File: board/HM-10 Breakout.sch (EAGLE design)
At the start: 19 parts, among them U1 V_REG_LDOSMD

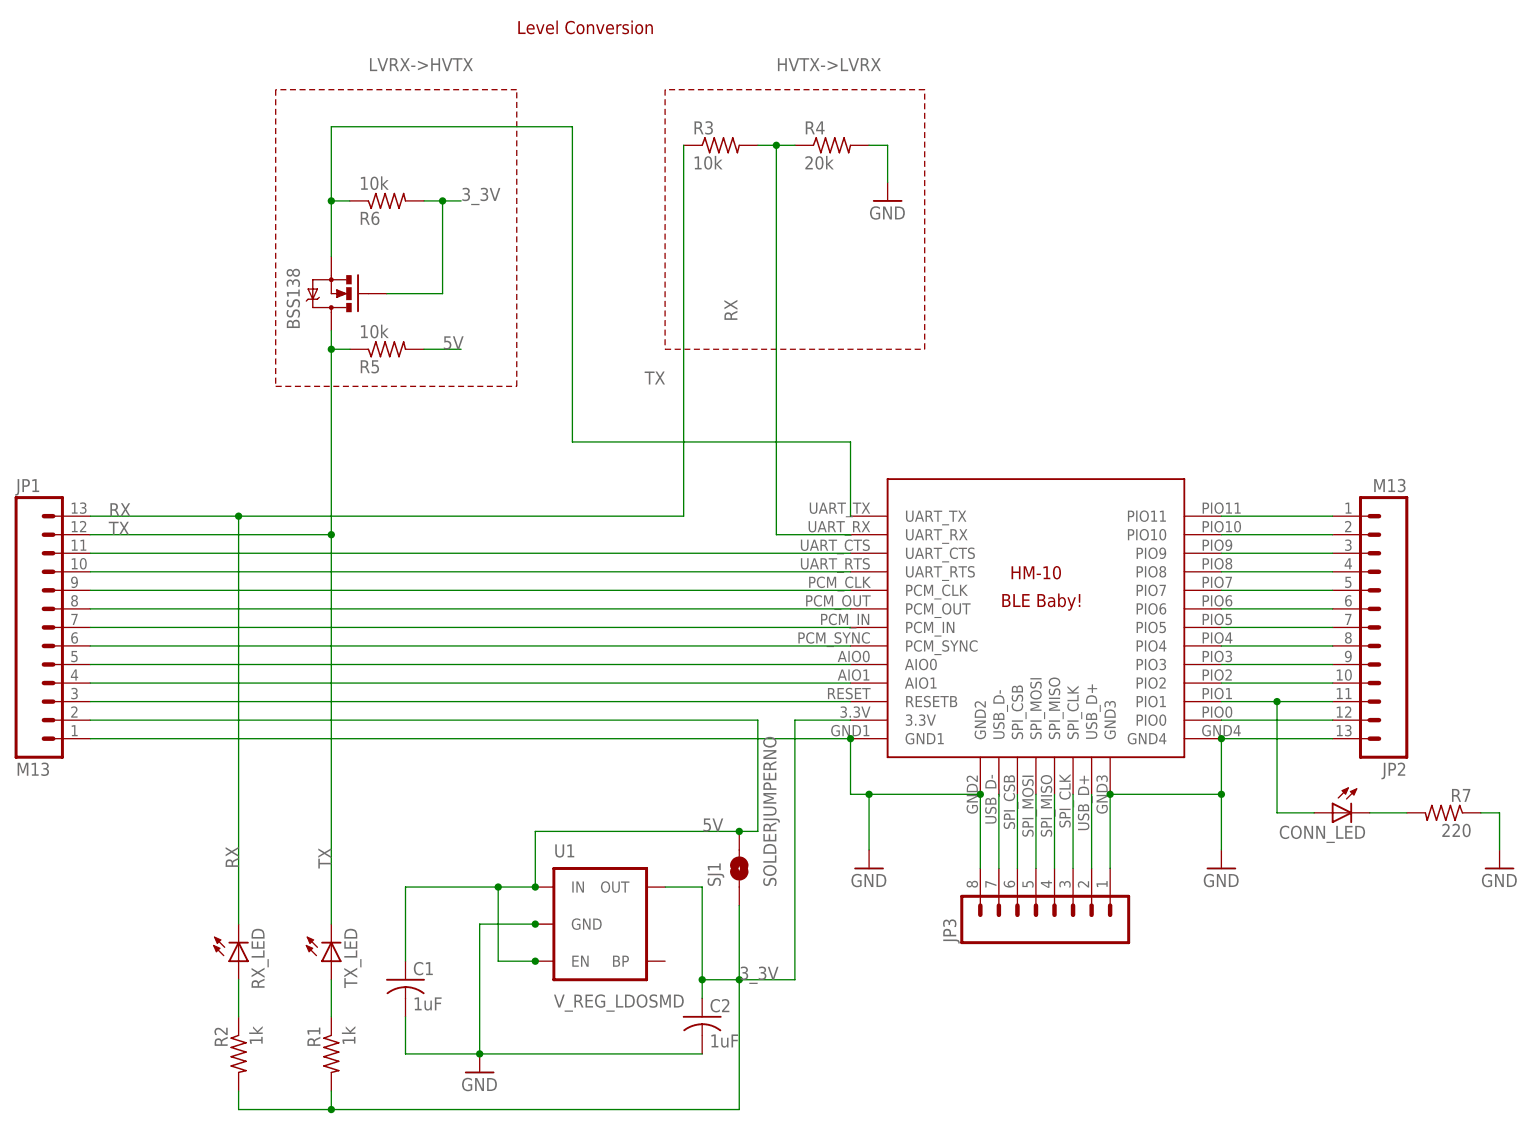
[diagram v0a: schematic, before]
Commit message: Overhaul PCB
Cleanup typography on silkscreen
Remove no connection lines
Replace HM-10 Eagle part with a more faithful version
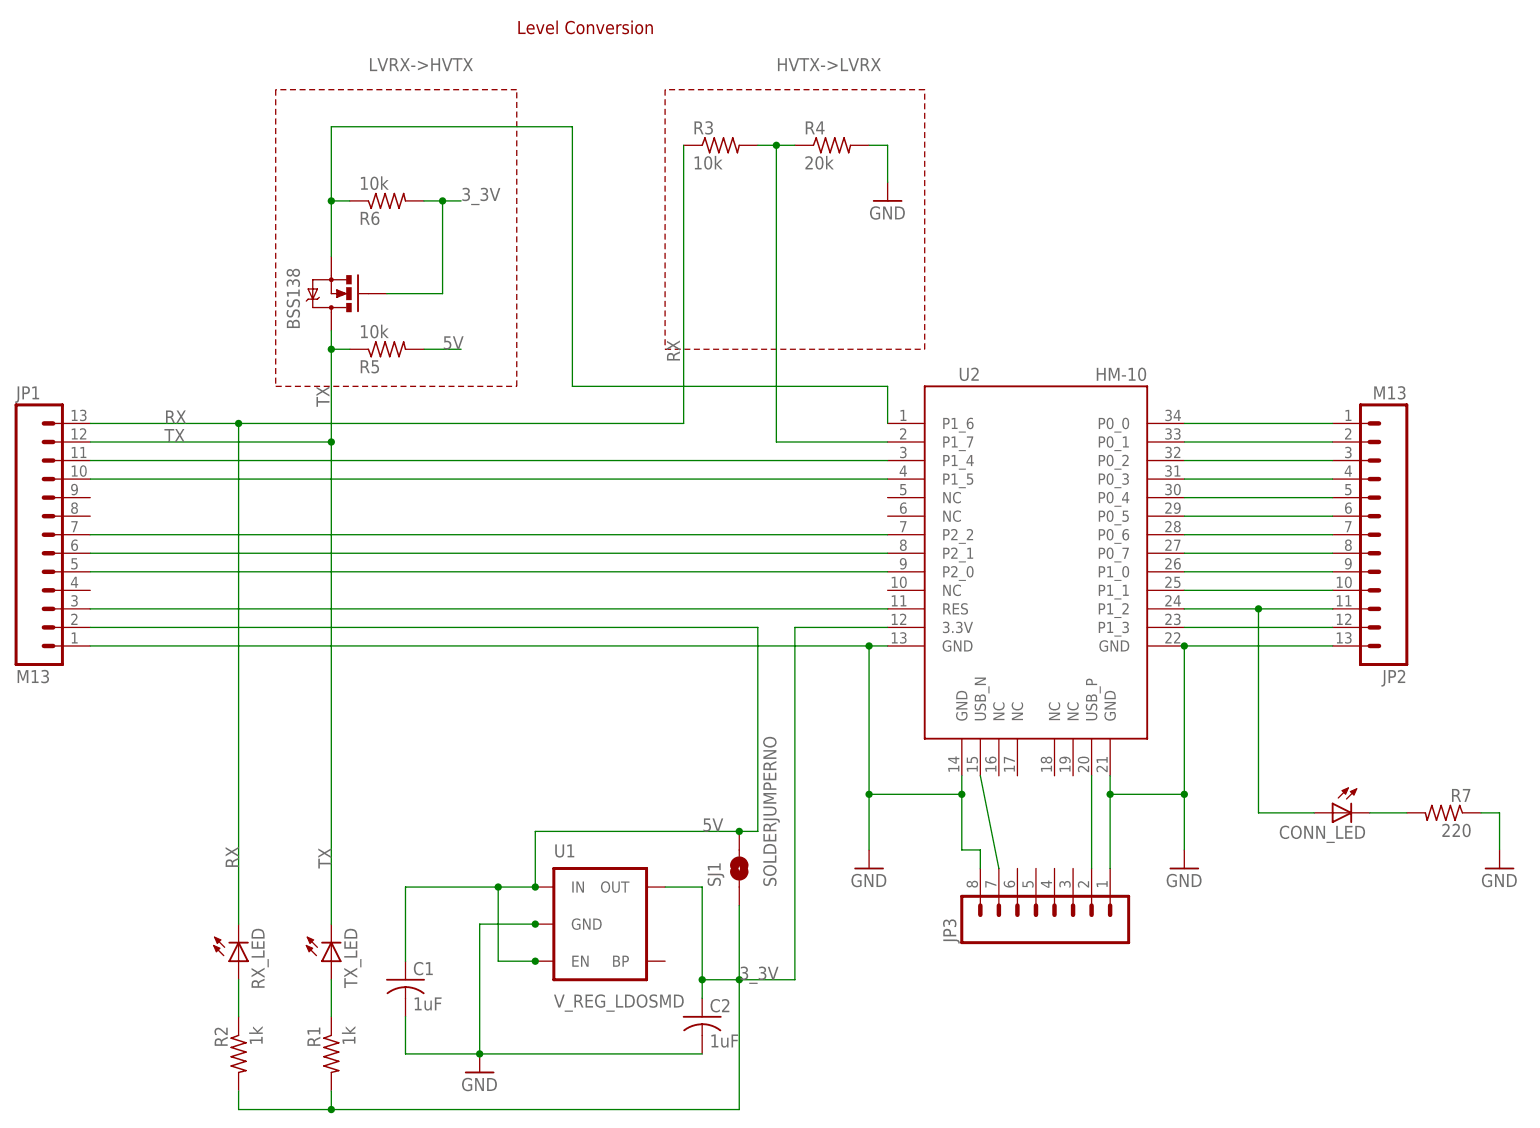
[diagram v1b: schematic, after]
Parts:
- removed U$1: BLE-HM-10, Random parts:BLE-HM-10
- added U2: HM-10, HM-10_BLE:HM-10
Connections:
- removed net N$25: JP2.12, U$1.PIO0
- removed net N$28: JP3.2, U$1.USB_D+
- removed net N$29: JP3.3, U$1.SPI_CLK
- removed net N$30: JP3.4, U$1.SPI_MISO
- removed net N$31: JP3.5, U$1.SPI_MOSI
- removed net N$32: JP3.6, U$1.SPI_CSB
- removed net N$33: JP3.7, U$1.USB_D-
- net 3_3V: now also U2.3.3V; no longer U$1.3.3V
- net GND: now also U2.GND@1, U2.GND@2, U2.GND@3, U2.GND@4; no longer U$1.GND1, U$1.GND2, U$1.GND3, U$1.GND4
- net HVTX->LVRX: now also U2.P1_7; no longer U$1.UART_RX
- net LVRX->HVTX: now also U2.P1_6; no longer U$1.UART_TX
- net N$10: now also U2.P1_5; no longer U$1.UART_RTS
- net N$11: now also U2.P1_4; no longer U$1.UART_CTS
- net N$14: now also JP2.9, U2.P1_0; no longer JP2.1, U$1.PIO11
- net N$15: now also JP2.8, U2.P0_7; no longer JP2.2, U$1.PIO10
- net N$16: now also JP2.7, U2.P0_6; no longer JP2.3, U$1.PIO9
- net N$17: now also JP2.6, U2.P0_5; no longer JP2.4, U$1.PIO8
- net N$18: now also U2.P0_4; no longer U$1.PIO7
- net N$19: now also JP2.4, U2.P0_3; no longer JP2.6, U$1.PIO6
- net N$2: now also U2.P1_2; no longer U$1.PIO1
- net N$20: now also JP2.3, U2.P0_2; no longer JP2.7, U$1.PIO5
- net N$21: now also JP2.2, U2.P0_1; no longer JP2.8, U$1.PIO4
- net N$22: now also JP2.1, U2.P0_0; no longer JP2.9, U$1.PIO3
- net N$23: now also JP2.12, U2.P1_3; no longer JP2.10, U$1.PIO2
- net N$3: now also U2.RES; no longer U$1.RESETB
- net N$4: now also JP3.7, U2.USB_N; no longer JP1.4, U$1.AIO1
- net N$5: now also JP1.7, U2.P2_2; no longer JP1.5, U$1.AIO0
- net N$6: now also JP1.5, U2.P2_0; no longer JP1.6, U$1.PCM_SYNC
- net N$7: now also JP1.6, U2.P2_1; no longer JP1.7, U$1.PCM_IN
- net N$8: now also JP2.10, U2.P1_1; no longer JP1.8, U$1.PCM_OUT
- net N$9: now also JP3.2, U2.USB_P; no longer JP1.9, U$1.PCM_CLK
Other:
- moved on the sheet: JP1, JP2

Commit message: Shrink board
Remove top row of pins
Change silkscreen to note change to SPI over USB
Add version number and text to silkscreen
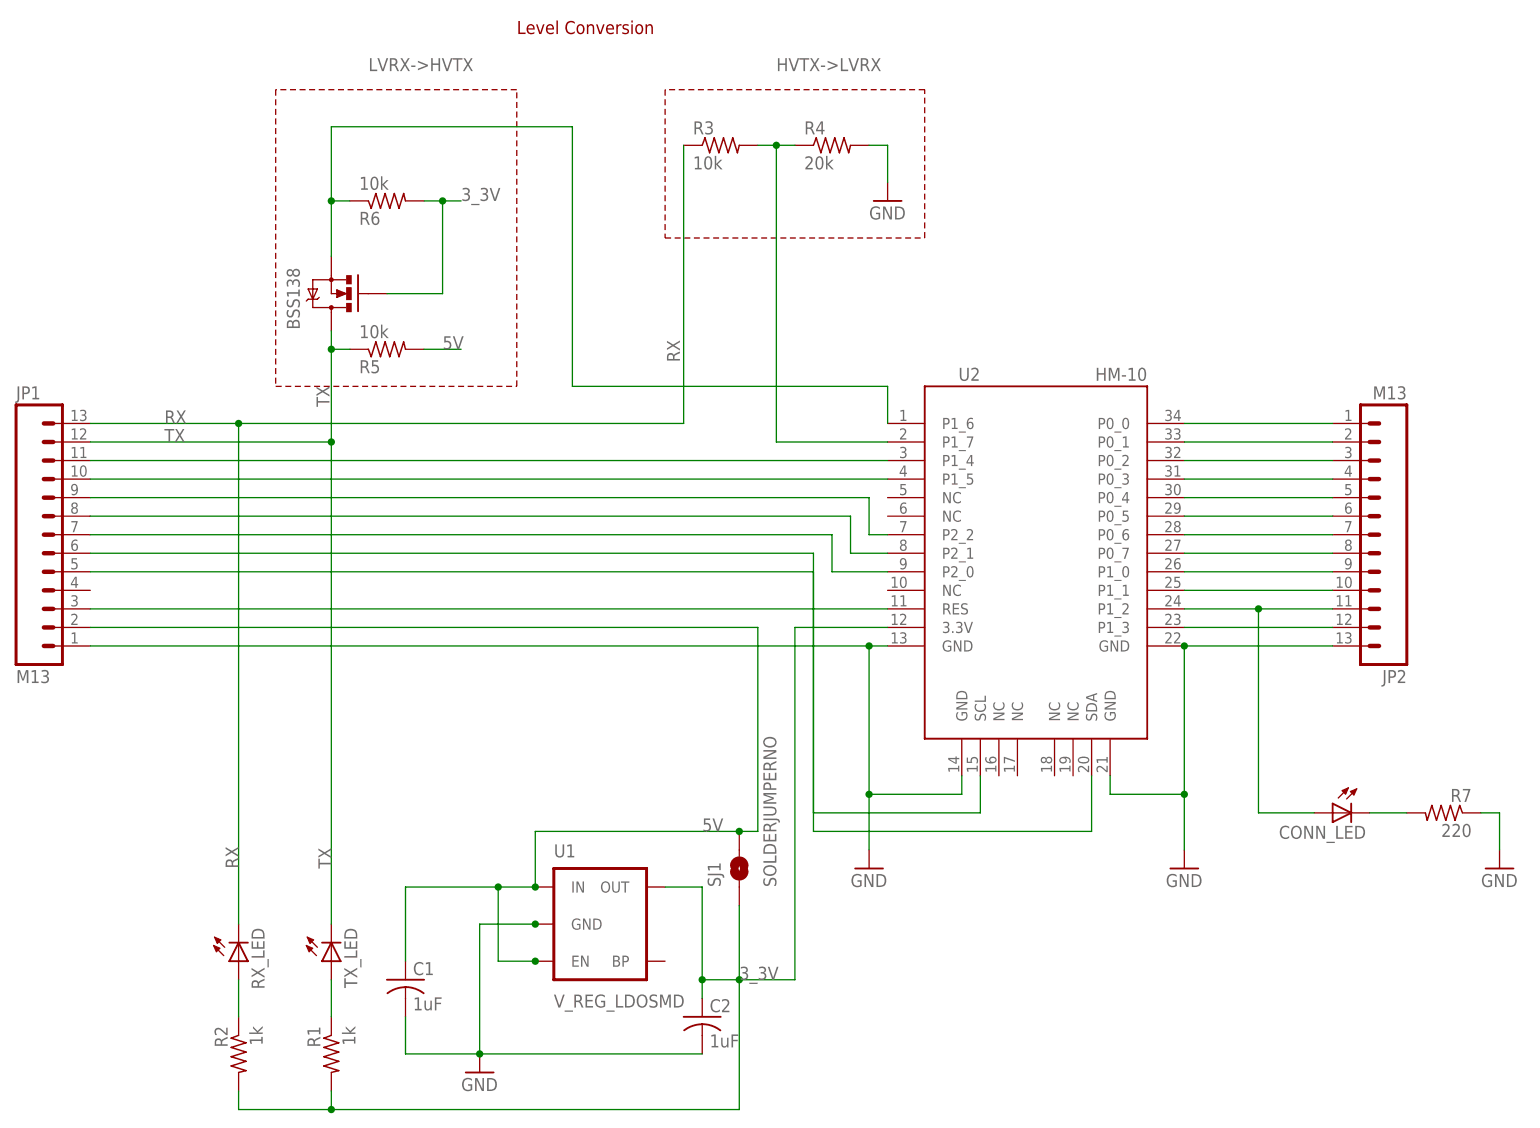
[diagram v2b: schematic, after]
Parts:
- removed JP3: (no value), SparkFun:M081X08
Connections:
- net GND: no longer JP3.1, JP3.8
- net N$4: now also JP1.5, U2.SCL; no longer JP3.7, U2.USB_N
- net N$5: now also JP1.9; no longer JP1.7
- net N$6: now also JP1.8, U2.P2_1; no longer JP1.5, U2.P2_0
- net N$7: now also JP1.7, U2.P2_0; no longer JP1.6, U2.P2_1
- net N$9: now also JP1.6, U2.SDA; no longer JP3.2, U2.USB_P
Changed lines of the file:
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@@
 <part name="JP1" library="SparkFun" deviceset="M13" device=""/>
 <part name="JP2" library="SparkFun" deviceset="M13" device=""/>
-<part name="JP3" library="SparkFun" deviceset="M08" device="1X08"/>
 <part name="GND1" library="SparkFun" deviceset="GND" device=""/>
 <part name="GND2" library="SparkFun" deviceset="GND" device=""/>
@@
 <wire x1="-2.54" y1="73.66" x2="-2.54" y2="114.3" width="0.1524" layer="94" style="shortdash"/>
 <wire x1="-2.54" y1="114.3" x2="-35.56" y2="114.3" width="0.1524" layer="94" style="shortdash"/>
-<wire x1="17.78" y1="114.3" x2="17.78" y2="78.74" width="0.1524" layer="94" style="shortdash"/>
-<wire x1="17.78" y1="78.74" x2="53.34" y2="78.74" width="0.1524" layer="94" style="shortdash"/>
-<wire x1="53.34" y1="78.74" x2="53.34" y2="114.3" width="0.1524" layer="94" style="shortdash"/>
+<wire x1="17.78" y1="114.3" x2="17.78" y2="93.98" width="0.1524" layer="94" style="shortdash"/>
+<wire x1="17.78" y1="93.98" x2="53.34" y2="93.98" width="0.1524" layer="94" style="shortdash"/>
+<wire x1="53.34" y1="93.98" x2="53.34" y2="114.3" width="0.1524" layer="94" style="shortdash"/>
 <wire x1="53.34" y1="114.3" x2="17.78" y2="114.3" width="0.1524" layer="94" style="shortdash"/>
 <text x="-2.54" y="121.92" size="1.778" layer="94">Level Conversion</text>
@@
 <instance part="JP1" gate="G$1" x="-71.12" y="53.34"/>
 <instance part="JP2" gate="G$1" x="119.38" y="53.34" rot="R180"/>
-<instance part="JP3" gate="G$1" x="71.12" y="2.54" rot="R90"/>
 <instance part="GND1" gate="1" x="45.72" y="7.62"/>
 <instance part="GND2" gate="1" x="88.9" y="7.62"/>
@@
 <pinref part="U2" gate="G$1" pin="GND@3"/>
 <wire x1="78.74" y1="20.32" x2="78.74" y2="17.78" width="0.1524" layer="91"/>
-<pinref part="JP3" gate="G$1" pin="1"/>
-<wire x1="78.74" y1="17.78" x2="78.74" y2="7.62" width="0.1524" layer="91"/>
-<junction x="78.74" y="17.78"/>
 </segment>
 <segment>
@@
 <wire x1="45.72" y1="10.16" x2="45.72" y2="17.78" width="0.1524" layer="91"/>
 <junction x="45.72" y="38.1"/>
-<pinref part="JP3" gate="G$1" pin="8"/>
 <pinref part="U2" gate="G$1" pin="GND@2"/>
 <wire x1="45.72" y1="17.78" x2="45.72" y2="38.1" width="0.1524" layer="91"/>
 <wire x1="58.42" y1="20.32" x2="58.42" y2="17.78" width="0.1524" layer="91"/>
-<wire x1="58.42" y1="17.78" x2="58.42" y2="10.16" width="0.1524" layer="91"/>
-<wire x1="58.42" y1="10.16" x2="60.96" y2="10.16" width="0.1524" layer="91"/>
-<wire x1="60.96" y1="10.16" x2="60.96" y2="7.62" width="0.1524" layer="91"/>
 <wire x1="58.42" y1="17.78" x2="45.72" y2="17.78" width="0.1524" layer="91"/>
-<junction x="58.42" y="17.78"/>
 <junction x="45.72" y="17.78"/>
 </segment>
@@
 </segment>
 </net>
-<net name="N$4" class="0">
-<segment>
-<pinref part="U2" gate="G$1" pin="USB_N"/>
-<pinref part="JP3" gate="G$1" pin="7"/>
-<wire x1="60.96" y1="20.32" x2="63.5" y2="7.62" width="0.1524" layer="91"/>
-</segment>
-</net>
-<net name="N$9" class="0">
-<segment>
-<pinref part="U2" gate="G$1" pin="USB_P"/>
-<pinref part="JP3" gate="G$1" pin="2"/>
-<wire x1="76.2" y1="20.32" x2="76.2" y2="7.62" width="0.1524" layer="91"/>
-</segment>
-</net>
 <net name="N$3" class="0">
 <segment>
@@
 </segment>
 </net>
-<net name="N$6" class="0">
-<segment>
-<pinref part="JP1" gate="G$1" pin="5"/>
-<pinref part="U2" gate="G$1" pin="P2_0"/>
-<wire x1="-60.96" y1="48.26" x2="48.26" y2="48.26" width="0.1524" layer="91"/>
-</segment>
-</net>
-<net name="N$7" class="0">
-<segment>
-<pinref part="U2" gate="G$1" pin="P2_1"/>
-<pinref part="JP1" gate="G$1" pin="6"/>
-<wire x1="48.26" y1="50.8" x2="-60.96" y2="50.8" width="0.1524" layer="91"/>
-</segment>
-</net>
-<net name="N$5" class="0">
-<segment>
-<pinref part="U2" gate="G$1" pin="P2_2"/>
-<pinref part="JP1" gate="G$1" pin="7"/>
-<wire x1="48.26" y1="53.34" x2="-60.96" y2="53.34" width="0.1524" layer="91"/>
-</segment>
-</net>
 <net name="N$8" class="0">
 <segment>
@@
 </segment>
 </net>
+<net name="N$4" class="0">
+<segment>
+<pinref part="U2" gate="G$1" pin="SCL"/>
+<wire x1="60.96" y1="20.32" x2="60.96" y2="15.24" width="0.1524" layer="91"/>
+<wire x1="60.96" y1="15.24" x2="38.1" y2="15.24" width="0.1524" layer="91"/>
+<wire x1="38.1" y1="15.24" x2="38.1" y2="48.26" width="0.1524" layer="91"/>
+<pinref part="JP1" gate="G$1" pin="5"/>
+<wire x1="38.1" y1="48.26" x2="-60.96" y2="48.26" width="0.1524" layer="91"/>
+</segment>
+</net>
+<net name="N$9" class="0">
+<segment>
+<pinref part="U2" gate="G$1" pin="SDA"/>
+<wire x1="76.2" y1="20.32" x2="76.2" y2="12.7" width="0.1524" layer="91"/>
+<wire x1="76.2" y1="12.7" x2="38.1" y2="12.7" width="0.1524" layer="91"/>
+<wire x1="38.1" y1="12.7" x2="38.1" y2="50.8" width="0.1524" layer="91"/>
+<pinref part="JP1" gate="G$1" pin="6"/>
+<wire x1="38.1" y1="50.8" x2="-60.96" y2="50.8" width="0.1524" layer="91"/>
+</segment>
+</net>
+<net name="N$5" class="0">
+<segment>
+<pinref part="U2" gate="G$1" pin="P2_2"/>
+<wire x1="48.26" y1="53.34" x2="45.72" y2="53.34" width="0.1524" layer="91"/>
+<wire x1="45.72" y1="53.34" x2="45.72" y2="58.42" width="0.1524" layer="91"/>
+<pinref part="JP1" gate="G$1" pin="9"/>
+<wire x1="45.72" y1="58.42" x2="-60.96" y2="58.42" width="0.1524" layer="91"/>
+</segment>
+</net>
+<net name="N$6" class="0">
+<segment>
+<pinref part="U2" gate="G$1" pin="P2_1"/>
+<wire x1="48.26" y1="50.8" x2="43.18" y2="50.8" width="0.1524" layer="91"/>
+<wire x1="43.18" y1="50.8" x2="43.18" y2="55.88" width="0.1524" layer="91"/>
+<pinref part="JP1" gate="G$1" pin="8"/>
+<wire x1="43.18" y1="55.88" x2="-60.96" y2="55.88" width="0.1524" layer="91"/>
+</segment>
+</net>
+<net name="N$7" class="0">
+<segment>
+<pinref part="U2" gate="G$1" pin="P2_0"/>
+<wire x1="48.26" y1="48.26" x2="40.64" y2="48.26" width="0.1524" layer="91"/>
+<wire x1="40.64" y1="48.26" x2="40.64" y2="53.34" width="0.1524" layer="91"/>
+<pinref part="JP1" gate="G$1" pin="7"/>
+<wire x1="40.64" y1="53.34" x2="-60.96" y2="53.34" width="0.1524" layer="91"/>
+</segment>
+</net>
